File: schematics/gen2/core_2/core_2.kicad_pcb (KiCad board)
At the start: 2 copper layers, 84.3 x 8.4 mm, 11 parts, among them U1 74LS04, U2 74LS574, U3 74LS02, U5 74LS00

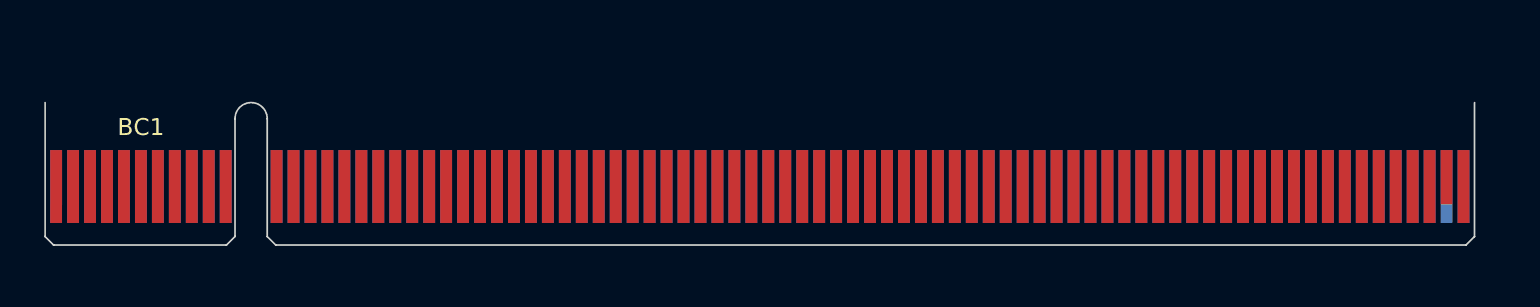
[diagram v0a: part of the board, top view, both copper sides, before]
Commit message: Add core3, fix core2
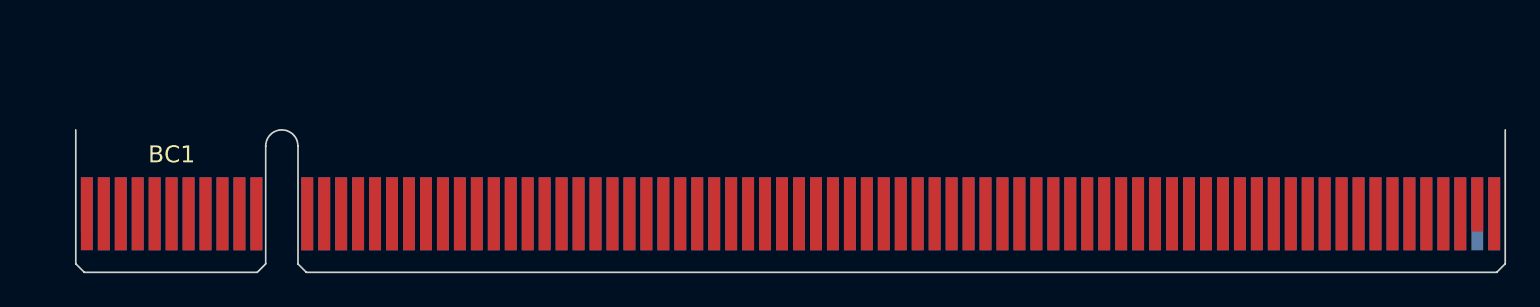
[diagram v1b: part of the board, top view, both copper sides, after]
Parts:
- moved BC1 2.42 mm to (87.0, 91.0)
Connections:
- BC1 pad A79: (no net) -> /STATE16
- BC1 pad B79: (no net) -> unconnected-(BC1-L4-PadB79)
- BC1 pad B80: (no net) -> unconnected-(BC1-R4-PadB80)
- TABLE8 pad 22: Net-(TABLE8-~{OE}) -> /STATE16
- U1 pad 2: Net-(TABLE8-~{OE}) -> /STATE16

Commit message: almost ready core 2
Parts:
- added C1: C, Capacitor_THT:C_Disc_D5.0mm_W2.5mm_P5.00mm, F.Cu at (227.9, 71.2)
- added C11: C, Capacitor_THT:C_Disc_D5.0mm_W2.5mm_P5.00mm, F.Cu at (251.9, 14.4)
- added C12: C, Capacitor_THT:C_Disc_D5.0mm_W2.5mm_P5.00mm, F.Cu at (279.8, 16.4)
- added C17: C, Capacitor_THT:C_Disc_D5.0mm_W2.5mm_P5.00mm, F.Cu at (260.9, 20.6)
- added C2: C, Capacitor_THT:C_Disc_D5.0mm_W2.5mm_P5.00mm, F.Cu at (196.0, 27.1)
- added C3: C, Capacitor_THT:C_Disc_D5.0mm_W2.5mm_P5.00mm, F.Cu at (280.5, 76.0)
- added C6: C, Capacitor_THT:C_Disc_D5.0mm_W2.5mm_P5.00mm, F.Cu at (235.9, 77.8)
- added C7: C, Capacitor_THT:C_Disc_D5.0mm_W2.5mm_P5.00mm, F.Cu at (232.6, 44.1)
- added C8: C, Capacitor_THT:C_Disc_D5.0mm_W2.5mm_P5.00mm, F.Cu at (232.6, 49.0)
- added C9: C, Capacitor_THT:C_Disc_D5.0mm_W2.5mm_P5.00mm, F.Cu at (233.0, 63.3)
- added R2: R, Resistor_THT:R_Axial_DIN0207_L6.3mm_D2.5mm_P7.62mm_Horizontal, F.Cu at (282.1, 21.0)
- moved U3 177.8 mm to (270.7, 19.7)
- moved B_IN0 167.6 mm to (242.7, 88.7), turned to 90 degrees
- moved U5 165.6 mm to (272.9, 80.2)
- moved U1 156.8 mm to (236.7, 16.7)
- moved B_IN1 145.9 mm to (236.6, 73.8), turned to 90 degrees
- moved B_OUT0 131.5 mm to (236.6, 61.8), turned to 90 degrees
- moved STEP1 130.9 mm to (248.7, 31.7), turned to 90 degrees
- moved U2 117.6 mm to (236.6, 49.8), turned to 90 degrees
- moved BC1 107.3 mm to (192.9, 108.1)
- moved TABLE7 94.9 mm to (225.0, 51.0), turned to -90 degrees
- moved TABLE8 73.4 mm to (225.0, 31.0), turned to -90 degrees
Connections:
- U3 pad 11: Net-(R3-Pad2) -> Net-(R2-Pad2)
- U3 pad 12: GND -> Net-(R2-Pad2)
- U3 pad 3: GND -> Net-(R2-Pad2)
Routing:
- net /STATE16: track 0.00 -> 185.0 mm, vias 0 -> 7
- net /~{LOAD_FR}: track 0.00 -> 159.4 mm, vias 0 -> 8
- net /~{IntDisable}: track 0.00 -> 149.4 mm, vias 0 -> 15
- net GND: track 0.00 -> 149.2 mm, vias 0 -> 9
- net /STATE10: track 0.00 -> 147.7 mm, vias 0 -> 11
- net /STATE11: track 0.00 -> 141.1 mm, vias 0 -> 7
- net /STATE14: track 0.00 -> 139.2 mm, vias 0 -> 2
- net /~CLK: track 0.00 -> 137.7 mm, vias 0 -> 3
- net /STATE13: track 0.00 -> 136.9 mm, vias 0 -> 3
- net /AddrDecrement: track 0.00 -> 136.8 mm, vias 0 -> 16
- net /STATE9: track 0.00 -> 131.1 mm, vias 0 -> 6
- net /STATE15: track 0.00 -> 130.3 mm, vias 0 -> 5
- net /STATE12: track 0.00 -> 129.2 mm, vias 0 -> 3
- net /STATE8: track 0.00 -> 124.3 mm, vias 0 -> 5
- net /IntEnable: track 0.00 -> 124.1 mm, vias 0 -> 9
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- added copper zone on B.Cu, net GND
- added copper zone on F.Cu, net VCC
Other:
- board size 84.3 x 8.4 mm -> 100 x 91.1 mm

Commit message: doine(core_ 2): almost ready to print
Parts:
- added C4: C, Capacitor_THT:C_Radial_D6.3mm_H5.0mm_P2.50mm, F.Cu at (195.2, 97.2)
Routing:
- net VCC: track 121.4 -> 148.1 mm, vias 8 -> 7
- net Net-(U5-Pad1): track 18.4 -> 23.6 mm
- net GND: track 149.2 -> 152.6 mm
- net /~{IntDisable}: track 149.4 -> 152.3 mm
- net Net-(B_IN0-A4): track 42.4 -> 44.6 mm, vias 0 -> 4
- net Net-(B_IN0-A3): track 42.4 -> 44.6 mm, vias 0 -> 2
- net /~{LOAD_FR}: track 159.4 -> 161.5 mm, vias 8 -> 10
- net /STATE0: track 93.5 -> 95.2 mm, vias 2 -> 6
- net /STATE13: track 136.9 -> 138.6 mm, vias 3 -> 4
- net /~{UPDATE_FR}: track 113.9 -> 115.4 mm, vias 6 -> 8
- net Net-(B_IN0-A2): track 42.4 -> 43.0 mm
- net Net-(STEP1-~{MR}): track 73.8 -> 74.3 mm, vias 1 -> 3
- net Net-(B_IN0-A7): track 42.4 -> 42.8 mm, vias 0 -> 2
- net Net-(B_IN0-A5): track 42.4 -> 42.8 mm, vias 0 -> 4
- net Net-(B_IN0-A6): track 42.4 -> 42.8 mm, vias 0 -> 4
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
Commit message: small changes
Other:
- board text added: "CORE 2"

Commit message: design + fix core_2
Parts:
- moved C2 37.9 mm to (228.8, 46.2), turned to -90 degrees
- moved C17 11.2 mm to (249.8, 20.8)
- moved C11 4.15 mm to (247.8, 14.2), turned to 0 degrees
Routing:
- net VCC: track 148.1 -> 92.7 mm, vias 7 -> 1
- net /STATE12: track 129.2 -> 132.2 mm
- net /STATE13: track 138.6 -> 141.5 mm
- net /STATE14: track 139.2 -> 141.5 mm
- net /AddrIncrement: track 106.2 -> 105.6 mm, vias 0 -> 2
- net /~{LOAD_FR}: vias 10 -> 12
- net /STATE15: vias 5 -> 9
- net /~{OUT_FR}: vias 5 -> 7
- net /~CLK: vias 3 -> 5

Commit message: update core_2
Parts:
- moved C17 0.79 mm to (250.5, 21.0)
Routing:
- net /~CLK: track 137.7 -> 138.6 mm, vias 5 -> 3
- net VCC: track 92.7 -> 93.4 mm
- net Net-(BC1-PULSE): vias 0 -> 2
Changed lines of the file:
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@@
 	(footprint "Capacitor_THT:C_Disc_D5.0mm_W2.5mm_P5.00mm"
 		(layer "F.Cu")
-		(at 249.75 20.75)
+		(at 250.5 21)
 		(descr "C, Disc series, Radial, pin pitch=5.00mm, diameter*width=5*2.5mm^2, Capacitor, http://cdn-reichelt.de/documents/datenblatt/B300/DS_KERKO_TC.pdf")
 		(tags "C Disc series Radial pin pitch 5.00mm diameter 5mm width 2.5mm Capacitor")
@@
 	)
 	(segment
+		(start 249.5 21)
+		(end 250.5 21)
+		(width 0.6)
+		(layer "F.Cu")
+		(net 6)
+	)
+	(segment
+		(start 248.7 21.8)
+		(end 249.5 21)
+		(width 0.6)
+		(layer "F.Cu")
+		(net 6)
+	)
+	(segment
 		(start 240.9 79.28)
 		(end 242.72 81.1)
@@
 	)
 	(segment
-		(start 248.7 21.8)
-		(end 249.75 20.75)
+		(start 248.7 24.1)
+		(end 248.7 21.8)
 		(width 0.6)
 		(layer "F.Cu")
@@
 	)
 	(segment
-		(start 248.7 24.1)
-		(end 248.7 21.8)
-		(width 0.6)
-		(layer "F.Cu")
-		(net 6)
-	)
-	(segment
 		(start 227.9 69.14)
 		(end 225 66.24)
@@
 	)
 	(segment
-		(start 280.5 82.7)
-		(end 282.402 84.602)
-		(width 0.2)
+		(start 278.05 101.5)
+		(end 270.5 101.5)
+		(width 0.4)
 		(layer "F.Cu")
 		(net 25)
 	)
 	(segment
-		(start 276.819 33.459)
-		(end 276.819 21.419)
-		(width 0.2)
+		(start 276.5 33.14)
+		(end 276.5 21.1)
+		(width 0.4)
 		(layer "F.Cu")
 		(net 25)
@@
 		(start 278.32 56)
 		(end 278.32 34.96)
-		(width 0.2)
+		(width 0.4)
 		(layer "F.Cu")
 		(net 25)
 	)
 	(segment
-		(start 278.32 34.96)
-		(end 276.819 33.459)
-		(width 0.2)
+		(start 283 85.2)
+		(end 283 96.55)
+		(width 0.4)
 		(layer "F.Cu")
 		(net 25)
 	)
 	(segment
-		(start 278.32 80.52)
-		(end 278.32 63.75)
-		(width 0.2)
+		(start 279.7 82.7)
+		(end 278.32 81.32)
+		(width 0.4)
 		(layer "F.Cu")
 		(net 25)
 	)
 	(segment
-		(start 282.402 96.698)
-		(end 278.5 100.6)
-		(width 0.2)
+		(start 283 96.55)
+		(end 278.05 101.5)
+		(width 0.4)
 		(layer "F.Cu")
 		(net 25)
@@
 	(segment
 		(start 280.5 82.7)
-		(end 278.32 80.52)
-		(width 0.2)
+		(end 283 85.2)
+		(width 0.4)
 		(layer "F.Cu")
 		(net 25)
 	)
 	(segment
-		(start 282.402 84.602)
-		(end 282.402 96.698)
-		(width 0.2)
+		(start 266.95 105.05)
+		(end 266.95 108.1)
+		(width 0.4)
 		(layer "F.Cu")
 		(net 25)
 	)
 	(segment
-		(start 276.4 100.6)
-		(end 271.5 100.6)
-		(width 0.2)
+		(start 280.5 82.7)
+		(end 279.7 82.7)
+		(width 0.4)
 		(layer "F.Cu")
 		(net 25)
 	)
 	(segment
-		(start 276.819 21.419)
-		(end 271.8 16.4)
-		(width 0.2)
+		(start 278.32 81.32)
+		(end 278.32 63.75)
+		(width 0.4)
 		(layer "F.Cu")
 		(net 25)
 	)
 	(segment
-		(start 266.95 105.15)
-		(end 266.95 108.1)
-		(width 0.2)
+		(start 270.5 101.5)
+		(end 266.95 105.05)
+		(width 0.4)
 		(layer "F.Cu")
 		(net 25)
 	)
 	(segment
-		(start 271.5 100.6)
-		(end 266.95 105.15)
-		(width 0.2)
+		(start 278.32 34.96)
+		(end 276.5 33.14)
+		(width 0.4)
 		(layer "F.Cu")
 		(net 25)
 	)
-	(via
-		(at 278.32 63.75)
-		(size 0.6)
-		(drill 0.3)
-		(layers "F.Cu" "B.Cu")
+	(segment
+		(start 276.5 21.1)
+		(end 271.8 16.4)
+		(width 0.4)
+		(layer "F.Cu")
 		(net 25)
 	)
 	(via
-		(at 278.32 56)
+		(at 278.32 63.75)
 		(size 0.6)
 		(drill 0.3)
@@
 	)
 	(via
-		(at 278.5 100.6)
+		(at 278.32 56)
 		(size 0.6)
 		(drill 0.3)
@@
 		(net 25)
 	)
-	(via
-		(at 276.4 100.6)
-		(size 0.6)
-		(drill 0.3)
-		(layers "F.Cu" "B.Cu")
-		(net 25)
-	)
-	(segment
-		(start 278.32 56)
-		(end 278.32 63.75)
-		(width 0.2)
-		(layer "B.Cu")
-		(net 25)
-	)
 	(segment
-		(start 278.5 100.6)
-		(end 276.4 100.6)
-		(width 0.2)
-		(layer "B.Cu")
-		(net 25)
-	)
-	(segment
-		(start 271.8 16.4)
-		(end 270.7 17.5)
-		(width 0.2)
+		(start 260.5 18.5)
+		(end 250.16 18.5)
+		(width 0.4)
 		(layer "B.Cu")
 		(net 25)
 	)
 	(segment
-		(start 260.5 18.5)
-		(end 249.577049 18.5)
-		(width 0.2)
+		(start 278.32 56)
+		(end 278.32 63.75)
+		(width 0.4)
 		(layer "B.Cu")
 		(net 25)
 	)
 	(segment
-		(start 249.577049 18.5)
-		(end 244.32 23.757049)
-		(width 0.2)
+		(start 262.5 16.5)
+		(end 260.5 18.5)
+		(width 0.4)
 		(layer "B.Cu")
 		(net 25)
 	)
 	(segment
-		(start 261.5 17.5)
-		(end 260.5 18.5)
-		(width 0.2)
+		(start 250.16 18.5)
+		(end 244.32 24.34)
+		(width 0.4)
 		(layer "B.Cu")
 		(net 25)
 	)
 	(segment
-		(start 270.7 17.5)
-		(end 261.5 17.5)
-		(width 0.2)
+		(start 271.7 16.5)
+		(end 262.5 16.5)
+		(width 0.4)
 		(layer "B.Cu")
 		(net 25)
 	)
 	(segment
-		(start 244.32 23.757049)
-		(end 244.32 24.34)
+		(start 271.8 16.4)
+		(end 271.7 16.5)
 		(width 0.2)
 		(layer "B.Cu")
@@
 	(segment
 		(start 272.88 90.32)
+		(end 272.88 87.78)
+		(width 0.2)
+		(layer "F.Cu")
+		(net 38)
+	)
+	(segment
+		(start 272.88 90.32)
 		(end 266.830057 96.369943)
 		(width 0.2)
@@
 	)
 	(segment
-		(start 272.88 90.32)
-		(end 272.88 87.78)
-		(width 0.2)
-		(layer "B.Cu")
-		(net 38)
-	)
-	(segment
 		(start 263.2 103.3)
 		(end 262.95 103.55)
@@
 	)
 	(segment
-		(start 275.657049 102.2)
-		(end 270.7 102.2)
+		(start 282.001 89.281)
+		(end 282.001 95.856049)
 		(width 0.2)
 		(layer "F.Cu")
@@
 	)
 	(segment
-		(start 282.001 89.281)
-		(end 282.001 95.856049)
+		(start 275 102.2)
+		(end 270.7 102.2)
 		(width 0.2)
 		(layer "F.Cu")
@@
 	(segment
 		(start 282.001 95.856049)
-		(end 275.657049 102.2)
+		(end 278.928524 98.928524)
 		(width 0.2)
 		(layer "F.Cu")
 		(net 91)
 	)
+	(via
+		(at 278.928524 98.928524)
+		(size 0.6)
+		(drill 0.3)
+		(layers "F.Cu" "B.Cu")
+		(net 91)
+	)
+	(via
+		(at 275 102.2)
+		(size 0.6)
+		(drill 0.3)
+		(layers "F.Cu" "B.Cu")
+		(net 91)
+	)
+	(segment
+		(start 278.928524 98.928524)
+		(end 275.657049 102.2)
+		(width 0.2)
+		(layer "B.Cu")
+		(net 91)
+	)
+	(segment
+		(start 275.657049 102.2)
+		(end 275 102.2)
+		(width 0.2)
+		(layer "B.Cu")
+		(net 91)
+	)
 	(segment
 		(start 241.65 73.81)
@@
 	)
 	(segment
+		(start 269.3 100.7)
+		(end 268.2 99.6)
+		(width 0.2)
+		(layer "F.Cu")
+		(net 131)
+	)
+	(segment
 		(start 209.8 46.2)
 		(end 209.76 46.24)
@@
 	)
 	(segment
+		(start 268.2 99.6)
+		(end 268.2 96.8)
+		(width 0.2)
+		(layer "F.Cu")
+		(net 131)
+	)
+	(segment
 		(start 268.2 75.2)
 		(end 268.2 67.7)
@@
 	)
 	(segment
-		(start 269.6 101)
-		(end 268.2 99.6)
-		(width 0.2)
-		(layer "F.Cu")
-		(net 131)
-	)
-	(segment
 		(start 269.46616 16.2)
 		(end 272.201 18.93484)
@@
 	)
 	(segment
-		(start 268.2 99.6)
-		(end 268.2 96.8)
-		(width 0.2)
-		(layer "F.Cu")
-		(net 131)
-	)
-	(segment
 		(start 209.599 29.499)
 		(end 209.303951 29.499)
@@
 	)
 	(via
-		(at 269.6 101)
+		(at 269.3 100.7)
 		(size 0.6)
 		(drill 0.3)
@@
 	)
 	(segment
-		(start 268.2 58.8)
-		(end 268.2 52.1)
+		(start 269.3 100.7)
+		(end 272.95 104.35)
 		(width 0.2)
 		(layer "B.Cu")
@@
 	)
 	(segment
-		(start 272.95 104.35)
-		(end 269.6 101)
+		(start 268.2 58.8)
+		(end 268.2 52.1)
 		(width 0.2)
 		(layer "B.Cu")
@@
 	)
 	(segment
-		(start 272.95 108.1)
-		(end 272.95 104.35)
+		(start 272.95 104.35)
+		(end 272.95 108.1)
 		(width 0.2)
 		(layer "B.Cu")

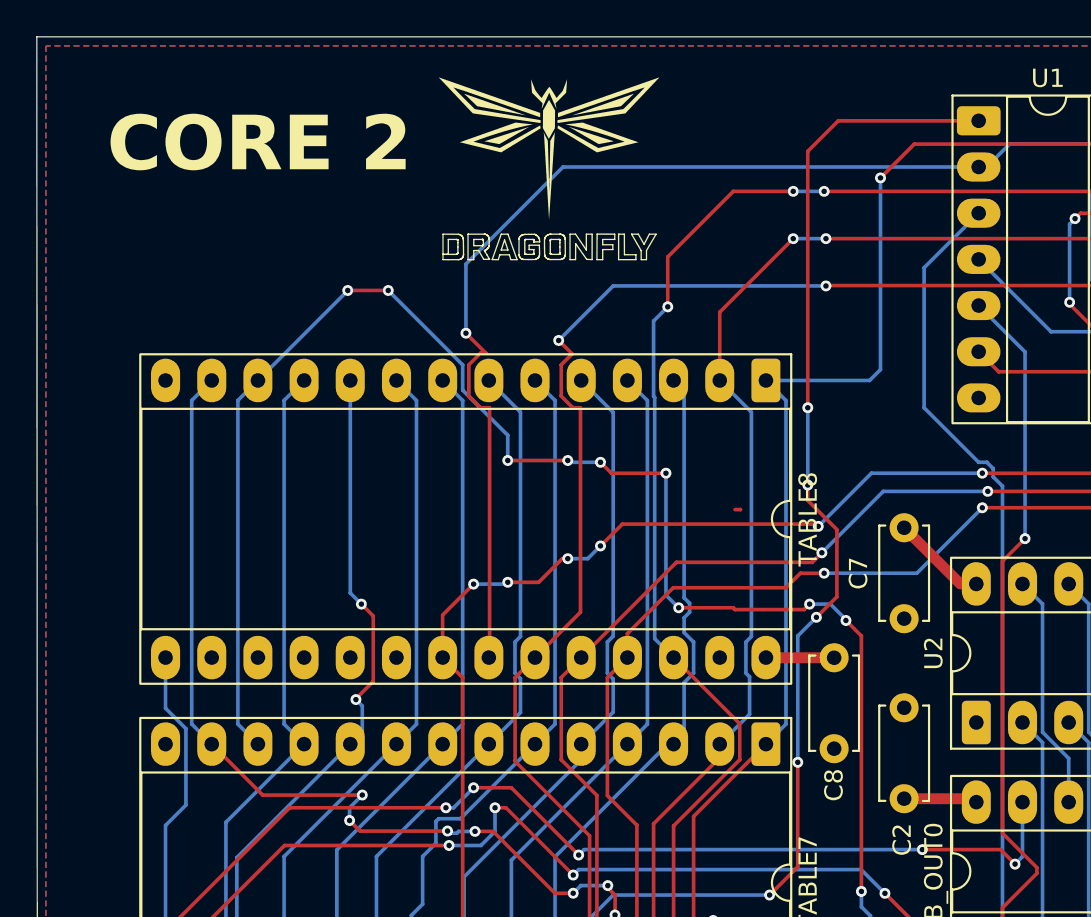
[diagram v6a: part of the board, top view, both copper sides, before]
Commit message: chore(core 2): changed logo and text
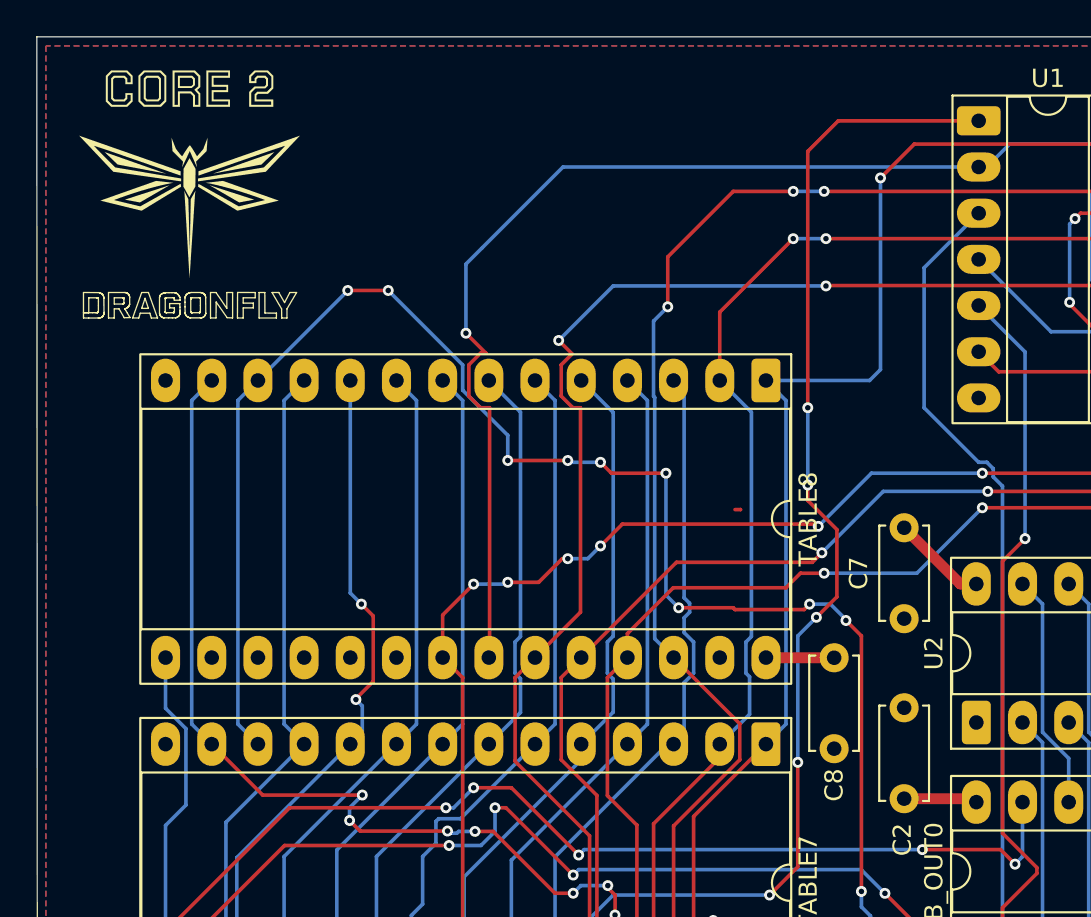
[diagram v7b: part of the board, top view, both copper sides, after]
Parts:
- added kibuzzard-6911C9E9: G***, kibuzzard-6911C9E9, F.Cu at (193.3, 14.9)
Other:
- board text removed: "CORE 2"

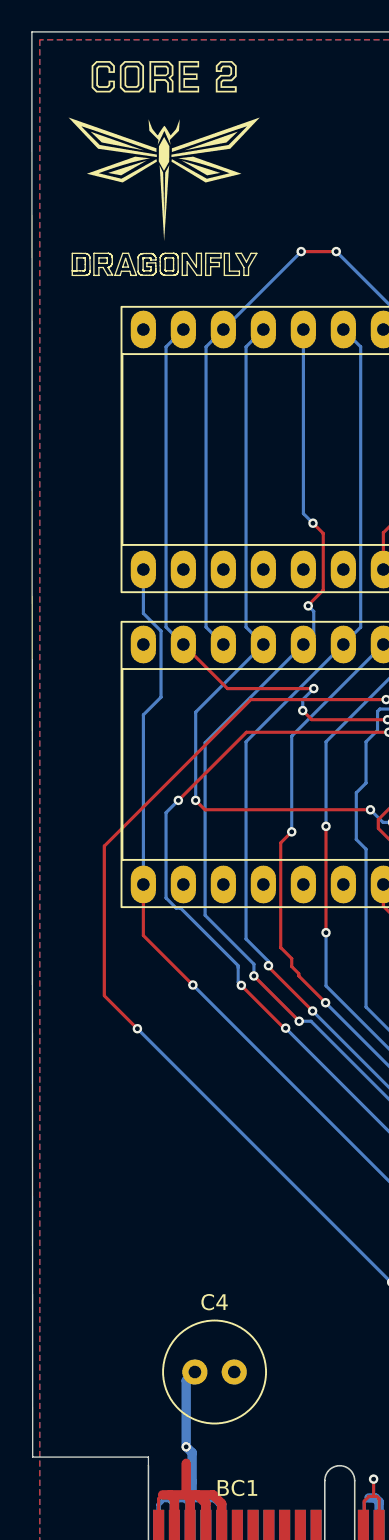
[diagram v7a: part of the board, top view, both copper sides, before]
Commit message: chore(kicad-pcb): added apps ucu logo
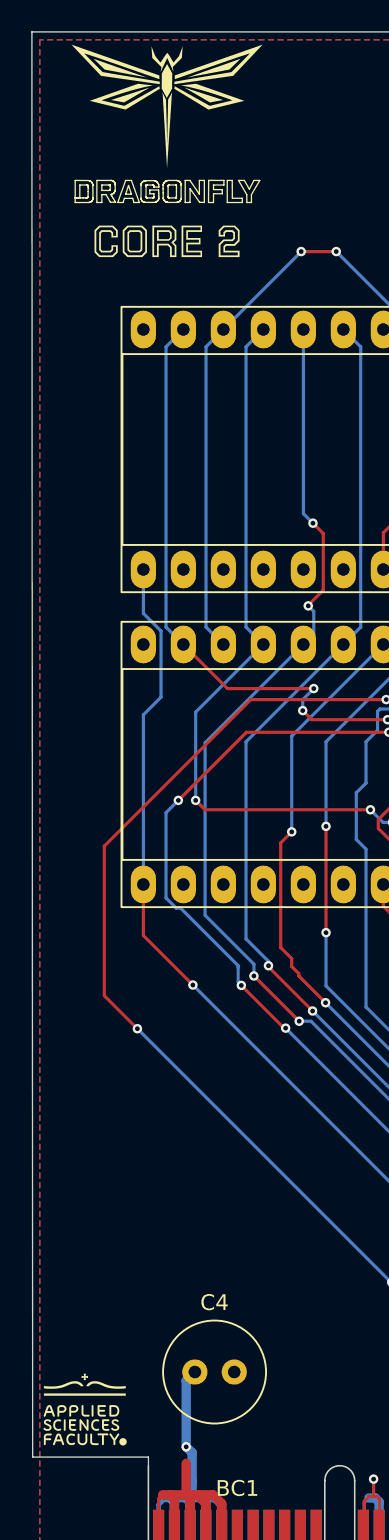
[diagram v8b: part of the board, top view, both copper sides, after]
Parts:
- moved kibuzzard-6911C9E9 10.5 mm to (193.5, 25.4)
